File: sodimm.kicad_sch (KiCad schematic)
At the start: 2 parts, among them J5 2309409-1

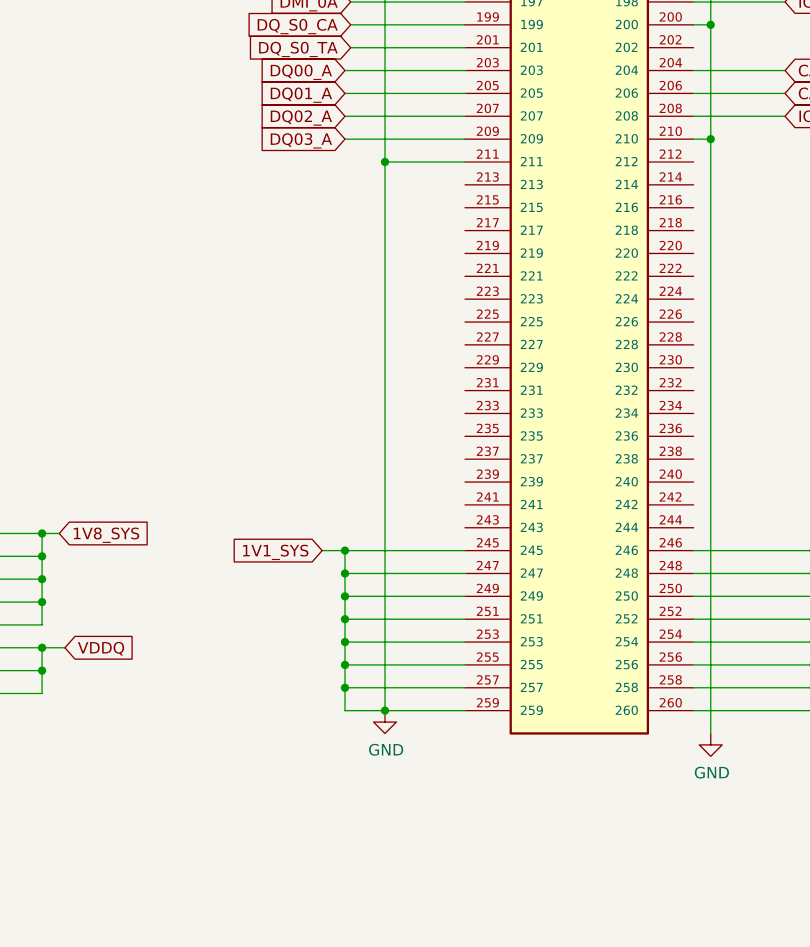
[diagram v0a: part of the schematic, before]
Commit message: Fix 1V1 connected to GND
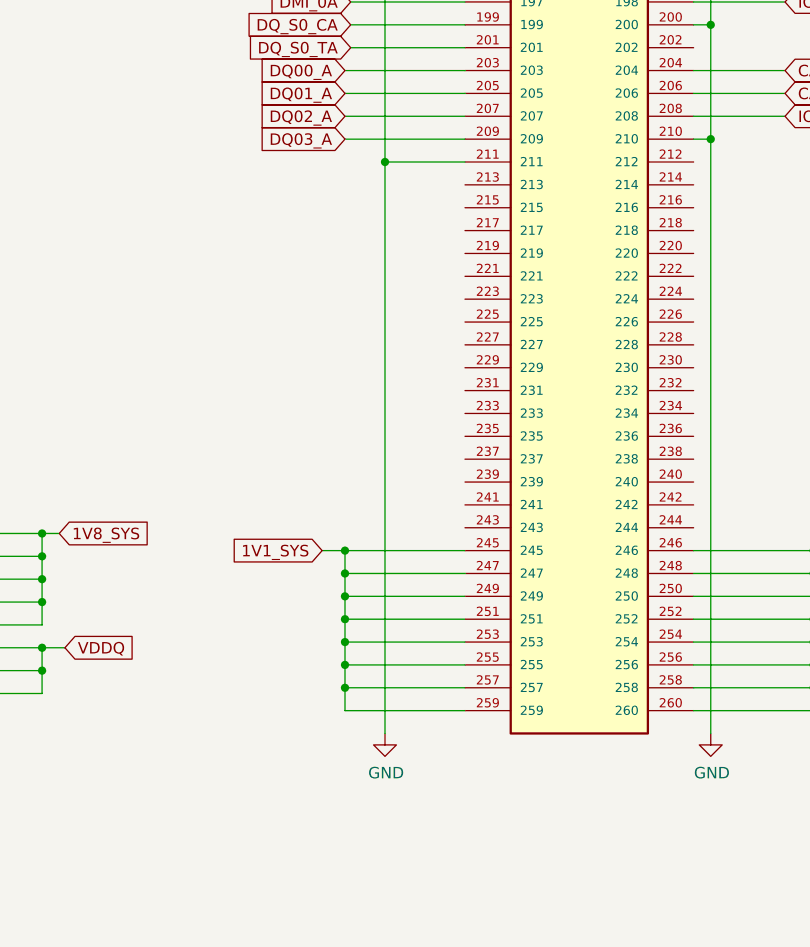
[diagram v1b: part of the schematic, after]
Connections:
- net GND: no longer J5.101, J5.103, J5.105, J5.107, J5.245, J5.247, J5.249, J5.251, J5.253, J5.255, J5.257, J5.259, J5.93, J5.95, J5.97, J5.99
- new net 1V1_SYS: J5.101, J5.103, J5.105, J5.107, J5.245, J5.247, J5.249, J5.251, J5.253, J5.255, J5.257, J5.259, J5.93, J5.95, J5.97, J5.99
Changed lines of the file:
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@@
   (junction (at 249.555 202.565) (diameter 0) (color 0 0 0 0)
   )
-  (junction (at 254 215.265) (diameter 0) (color 0 0 0 0)
-  )
   (junction (at 208.28 68.58) (diameter 0) (color 0 0 0 0)
   )
@@
     (stroke (width 0) (type default) (color 0 0 0 0))
   )
-  (wire (pts (xy 254 154.305) (xy 254 215.265))
-    (stroke (width 0) (type default) (color 0 0 0 0))
-  )
   (wire (pts (xy 254 90.805) (xy 254 111.125))
     (stroke (width 0) (type default) (color 0 0 0 0))
@@
     (stroke (width 0) (type default) (color 0 0 0 0))
   )
-  (wire (pts (xy 254 215.265) (xy 249.555 215.265))
+  (wire (pts (xy 249.555 215.265) (xy 262.89 215.265))
     (stroke (width 0) (type default) (color 0 0 0 0))
   )
@@
     (stroke (width 0) (type default) (color 0 0 0 0))
   )
+  (wire (pts (xy 254 154.305) (xy 254 217.805))
+    (stroke (width 0) (type default) (color 0 0 0 0))
+  )
   (wire (pts (xy 202.565 200.66) (xy 215.9 200.66))
     (stroke (width 0) (type default) (color 0 0 0 0))
@@
   )
   (wire (pts (xy 177.165 167.64) (xy 163.83 167.64))
-    (stroke (width 0) (type default) (color 0 0 0 0))
-  )
-  (wire (pts (xy 262.89 215.265) (xy 254 215.265))
     (stroke (width 0) (type default) (color 0 0 0 0))
   )
@@
     (pin "1")
   )
-  (symbol (lib_id "lpddr4-test-board:GND") (at 254 215.265 0) (unit 1)
+  (symbol (lib_id "lpddr4-test-board:GND") (at 254 217.805 0) (unit 1)
     (in_bom yes) (on_board yes)
-    (property "Reference" "#PWR0103" (id 0) (at 254 221.615 0)
-      (effects (font (size 1.27 1.27)) hide)
-    )
-    (property "Value" "GND" (id 1) (at 254.127 219.6592 0))
-    (property "Footprint" "" (id 2) (at 254 215.265 0)
-      (effects (font (size 1.27 1.27)) hide)
-    )
-    (property "Datasheet" "" (id 3) (at 254 215.265 0)
-      (effects (font (size 1.27 1.27)) hide)
-    )
+    (property "Reference" "#PWR0103" (id 0) (at 254 224.155 0)
+      (effects (font (size 1.27 1.27)) hide)
+    )
+    (property "Value" "GND" (id 1) (at 254.127 222.1992 0))
+    (property "Footprint" "" (id 2) (at 254 217.805 0)
+      (effects (font (size 1.27 1.27)) hide)
+    )
+    (property "Datasheet" "" (id 3) (at 254 217.805 0)
+      (effects (font (size 1.27 1.27)) hide)
+    )

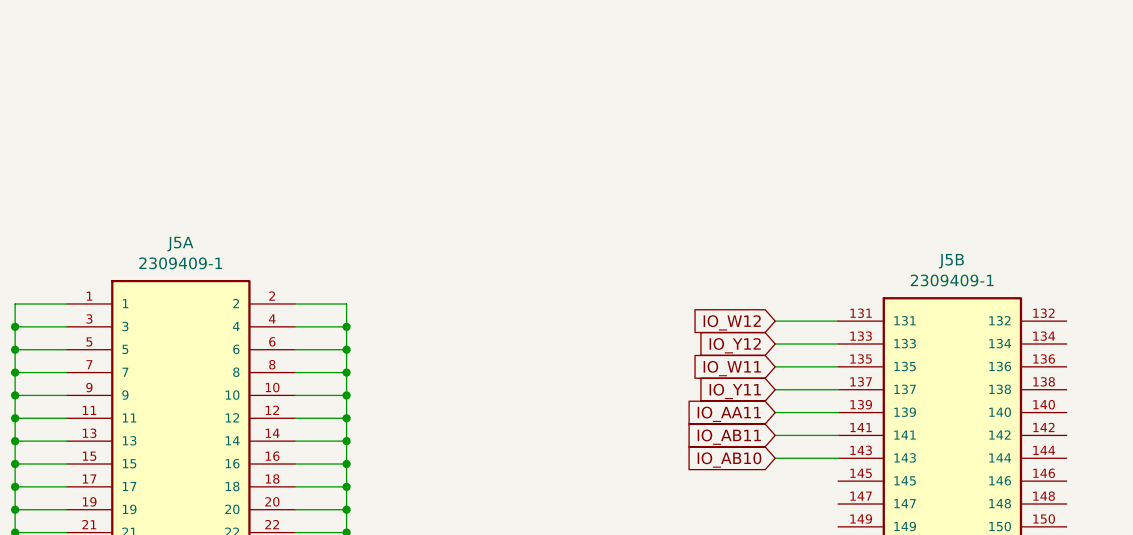
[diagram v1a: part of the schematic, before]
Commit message: Placement and routing of FT4232H. Re annotation of the schematics
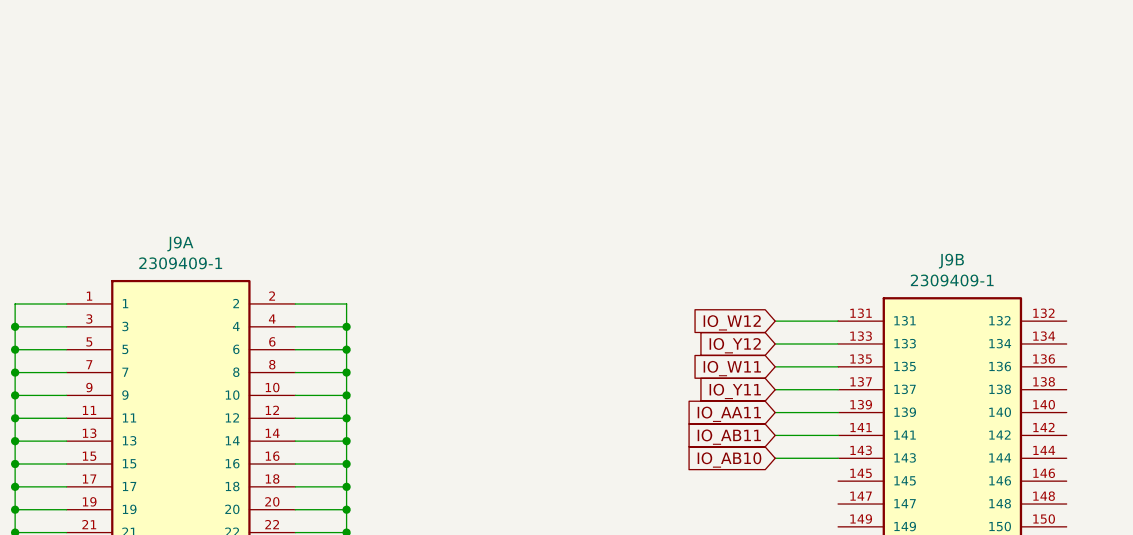
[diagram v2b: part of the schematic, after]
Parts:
- renumbered J5 to J9
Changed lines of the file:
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@@
   (symbol (lib_id "lpddr4-test-board:GND") (at 158.115 111.76 0) (unit 1)
     (in_bom yes) (on_board yes)
-    (property "Reference" "#PWR0230" (id 0) (at 158.115 118.11 0)
+    (property "Reference" "#PWR0220" (id 0) (at 158.115 118.11 0)
       (effects (font (size 1.27 1.27)) hide)
     )
@@
   (symbol (lib_id "lpddr4-test-board:2309409-1") (at 189.865 134.62 0) (unit 1)
     (in_bom yes) (on_board yes)
-    (property "Reference" "J5" (id 0) (at 189.865 44.0182 0))
+    (property "Reference" "J9" (id 0) (at 189.865 44.0182 0))
     (property "Value" "2309409-1" (id 1) (at 189.865 46.3296 0))
     (property "Footprint" "lpddr4-test-board-footprints:TE_2309409-1" (id 2) (at 182.245 226.06 0)
@@
   (symbol (lib_id "lpddr4-test-board:2309409-1") (at 275.59 133.985 0) (unit 2)
     (in_bom yes) (on_board yes)
-    (property "Reference" "J5" (id 0) (at 275.59 45.9232 0))
+    (property "Reference" "J9" (id 0) (at 275.59 45.9232 0))
     (property "Value" "2309409-1" (id 1) (at 275.59 48.2346 0))
     (property "Footprint" "lpddr4-test-board-footprints:TE_2309409-1" (id 2) (at 267.97 225.425 0)
@@
   (symbol (lib_id "lpddr4-test-board:GND") (at 290.195 217.805 0) (unit 1)
     (in_bom yes) (on_board yes)
-    (property "Reference" "#PWR0108" (id 0) (at 290.195 224.155 0)
+    (property "Reference" "#PWR0224" (id 0) (at 290.195 224.155 0)
       (effects (font (size 1.27 1.27)) hide)
     )
@@
   (symbol (lib_id "lpddr4-test-board:GND") (at 254 217.805 0) (unit 1)
     (in_bom yes) (on_board yes)
-    (property "Reference" "#PWR0103" (id 0) (at 254 224.155 0)
+    (property "Reference" "#PWR0223" (id 0) (at 254 224.155 0)
       (effects (font (size 1.27 1.27)) hide)
     )
@@
   (symbol (lib_id "lpddr4-test-board:GND") (at 215.9 111.76 0) (unit 1)
     (in_bom yes) (on_board yes)
-    (property "Reference" "#PWR0179" (id 0) (at 215.9 118.11 0)
+    (property "Reference" "#PWR0222" (id 0) (at 215.9 118.11 0)
       (effects (font (size 1.27 1.27)) hide)
     )
@@
   (symbol (lib_id "lpddr4-test-board:GND") (at 205.105 220.98 0) (unit 1)
     (in_bom yes) (on_board yes)
-    (property "Reference" "#PWR0180" (id 0) (at 205.105 227.33 0)
-      (effects (font (size 1.27 1.27)) hide)
-    )
+    (property "Reference" "#PWR0221" (id 0) (at 205.105 227.33 0)
+      (effects (font (size 1.27 1.27)) hide)
+    )
